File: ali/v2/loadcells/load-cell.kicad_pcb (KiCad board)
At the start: 4 copper layers, 85 x 76 mm, 108 parts, among them J1 Conn_02x01, J10 Conn_01x04, J11 Conn_01x04, J12 Conn_01x04, J2 Conn_01x05, J26 Vertical Ethernet, J3 USB_C_Receptacle_USB2.0_16P, J4 Conn_01x15, J5 Conn_02x09_Counter_Clockwise, J6 Screw_Terminal_01x02, J8 Conn_01x03, J9 Conn_01x04, SW1 SKRPANE010, U1 STM32H563RIV6, U2 AP2112K-3.3, U4 TJA1462ATK, U6 ADS124S08, U7 LAN8742AI, Y1 25 MHz, Y2 25 MHz

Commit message: Update LCs to have 6 inputs instead of 4
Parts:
- removed J10, J11, J9: Conn_01x04, APRL_Connector_Molex:Molex_CLIK-Mate_503159-0401_1x04-1MP_P1.50mm_Vertical
- added C51: 1nF, APRL_Passive:C_0603, F.Cu at (106.5, 80.5)
- added C52: 1nF, APRL_Passive:C_0603, F.Cu at (106.5, 74.8)
- added C53: 1nF, APRL_Passive:C_0603, F.Cu at (106.5, 99.7)
- added C54: 1nF, APRL_Passive:C_0603, F.Cu at (106.5, 93.7)
- added C55: 10nF, APRL_Passive:C_0603, F.Cu at (108.7, 77.5)
- added C56: 10nF, APRL_Passive:C_0603, F.Cu at (108.7, 96.7)
- added J13: Conn_01x04, APRL_Connector_Molex:Molex_CLIK-Mate_503159-0401_1x04-1MP_P1.50mm_Vertical, F.Cu at (98.9, 113.6)
- added J14: Conn_01x04, APRL_Connector_Molex:Molex_CLIK-Mate_503159-0401_1x04-1MP_P1.50mm_Vertical, F.Cu at (98.9, 104.1)
- added J15: Conn_01x04, APRL_Connector_Molex:Molex_CLIK-Mate_503159-0401_1x04-1MP_P1.50mm_Vertical, F.Cu at (99.0, 84.8)
- added J16: Conn_01x04, APRL_Connector_Molex:Molex_CLIK-Mate_503159-0401_1x04-1MP_P1.50mm_Vertical, F.Cu at (98.9, 75.2)
- added J17: Conn_01x04, APRL_Connector_Molex:Molex_CLIK-Mate_503159-0401_1x04-1MP_P1.50mm_Vertical, F.Cu at (98.9, 94.4)
- added R32: 4.7k, APRL_Passive:R_0603, F.Cu at (106.5, 78.5)
- added R33: 4.7k, APRL_Passive:R_0603, F.Cu at (106.5, 76.5)
- added R34: 4.7k, APRL_Passive:R_0603, F.Cu at (106.5, 97.7)
- added R35: 4.7k, APRL_Passive:R_0603, F.Cu at (106.5, 95.7)
- moved C37 13.2 mm to (106.5, 109.3), turned to 0 degrees
- moved R24 12.8 mm to (106.5, 107.3)
- moved C39 12.6 mm to (108.7, 106.3), turned to 90 degrees
- moved R25 12.4 mm to (106.5, 105.3)
- moved C38 12.0 mm to (106.5, 103.3), turned to 180 degrees
- moved C42 8.92 mm to (106.5, 118.9), turned to 0 degrees
- moved R26 8.53 mm to (106.5, 116.9)
- moved C44 8.33 mm to (108.7, 115.9), turned to 90 degrees
- moved R27 8.13 mm to (106.5, 114.9)
- moved C34 7.80 mm to (106.5, 90.1), turned to 0 degrees
- moved C43 7.73 mm to (106.5, 112.9), turned to 180 degrees
- moved R22 7.40 mm to (106.5, 88.1)
- moved C35 7.20 mm to (108.7, 87.1), turned to 90 degrees
- moved R23 7.00 mm to (106.5, 86.1)
- moved C36 6.61 mm to (106.5, 84.1), turned to 180 degrees
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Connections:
- C34 pad 1: Net-(U6-GPIO0/AIN8) -> GND
- C34 pad 2: GND -> Net-(U6-GPIO0/AIN8)
- C35 pad 1: Net-(U6-GPIO1/AIN9) -> Net-(U6-GPIO0/AIN8)
- C35 pad 2: Net-(U6-GPIO0/AIN8) -> Net-(U6-GPIO1/AIN9)
- C36 pad 1: GND -> Net-(U6-GPIO1/AIN9)
- C36 pad 2: Net-(U6-GPIO1/AIN9) -> GND
- C37 pad 1: Net-(U6-AIN4) -> GND
- C37 pad 2: GND -> Net-(U6-AIN4)
- C38 pad 1: GND -> Net-(U6-AIN5)
- C38 pad 2: Net-(U6-AIN5) -> GND
- C39 pad 1: Net-(U6-AIN5) -> Net-(U6-AIN4)
- C39 pad 2: Net-(U6-AIN4) -> Net-(U6-AIN5)
- C42 pad 1: Net-(U6-AIN2) -> GND
- C42 pad 2: GND -> Net-(U6-AIN2)
- C43 pad 1: GND -> Net-(U6-AIN3)
- C43 pad 2: Net-(U6-AIN3) -> GND
- C44 pad 1: Net-(U6-AIN3) -> Net-(U6-AIN2)
- C44 pad 2: Net-(U6-AIN2) -> Net-(U6-AIN3)
- C45 pad 1: Net-(U6-AIN0) -> GND
- C45 pad 2: GND -> Net-(U6-AIN0)
- C46 pad 1: GND -> Net-(U6-AIN1)
- C46 pad 2: Net-(U6-AIN1) -> GND
- C47 pad 1: Net-(U6-AIN1) -> Net-(U6-AIN0)
- C47 pad 2: Net-(U6-AIN0) -> Net-(U6-AIN1)
- J12 pad 1: +5V -> GND
- J12 pad 4: GND -> +5V
- R28 pad 1: Net-(J12-Pin_2) -> Net-(J12-Pin_3)
- R29 pad 1: Net-(J12-Pin_3) -> Net-(J12-Pin_2)
- U6 pad 19: unconnected-(U6-GPIO3/AIN11-Pad19) -> Net-(U6-GPIO3/AIN11)
- U6 pad 20: unconnected-(U6-GPIO2/AIN10-Pad20) -> Net-(U6-GPIO2/AIN10)
- U6 pad 31: unconnected-(U6-REFN1/AIN7-Pad31) -> Net-(U6-REFN1/AIN7)
- U6 pad 32: unconnected-(U6-REFP1/AIN6-Pad32) -> Net-(U6-REFP1/AIN6)
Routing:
- net Net-(U6-REFP1/AIN6): track 0.00 -> 24.0 mm
- net Net-(U6-REFN1/AIN7): track 0.00 -> 23.0 mm
- net Net-(U6-GPIO3/AIN11): track 0.00 -> 20.7 mm
- net Net-(U6-GPIO2/AIN10): track 0.00 -> 20.1 mm
- net Net-(U6-AIN4): track 21.1 -> 33.1 mm
- net Net-(U6-AIN5): track 19.3 -> 31.3 mm
- net Net-(U6-AIN2): track 35.5 -> 43.3 mm
- net Net-(U6-GPIO0/AIN8): track 18.3 -> 25.9 mm
- net Net-(U6-AIN3): track 33.8 -> 41.3 mm
- net Net-(U6-GPIO1/AIN9): track 19.0 -> 26.0 mm
- net Net-(J17-Pin_3): track 0.00 -> 6.92 mm
- net Net-(J16-Pin_3): track 0.00 -> 6.92 mm
- net +5V: track 86.6 -> 91.5 mm
- net Net-(J17-Pin_2): track 0.00 -> 4.92 mm
- net Net-(J16-Pin_2): track 0.00 -> 4.92 mm
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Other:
- board text added: "L5"
- board text added: "L6"

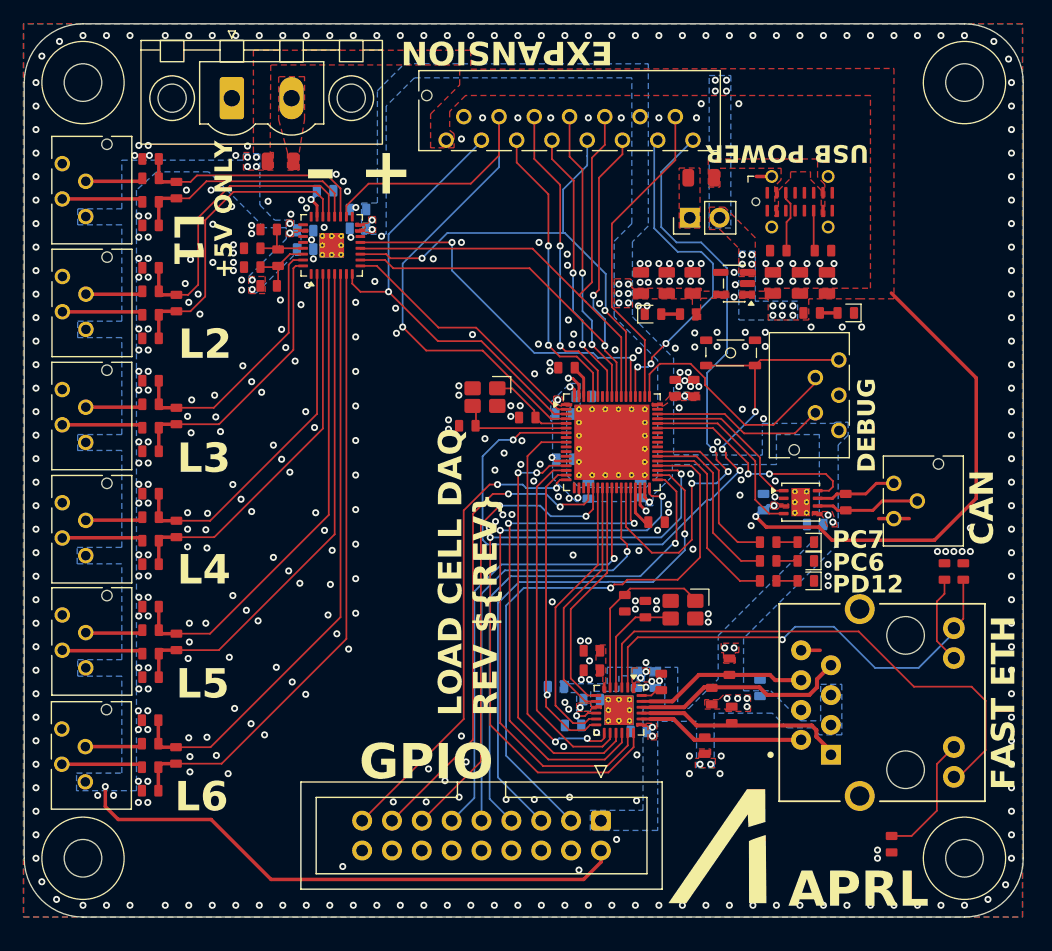
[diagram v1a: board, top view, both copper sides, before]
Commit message: Use 1206 on AFEs
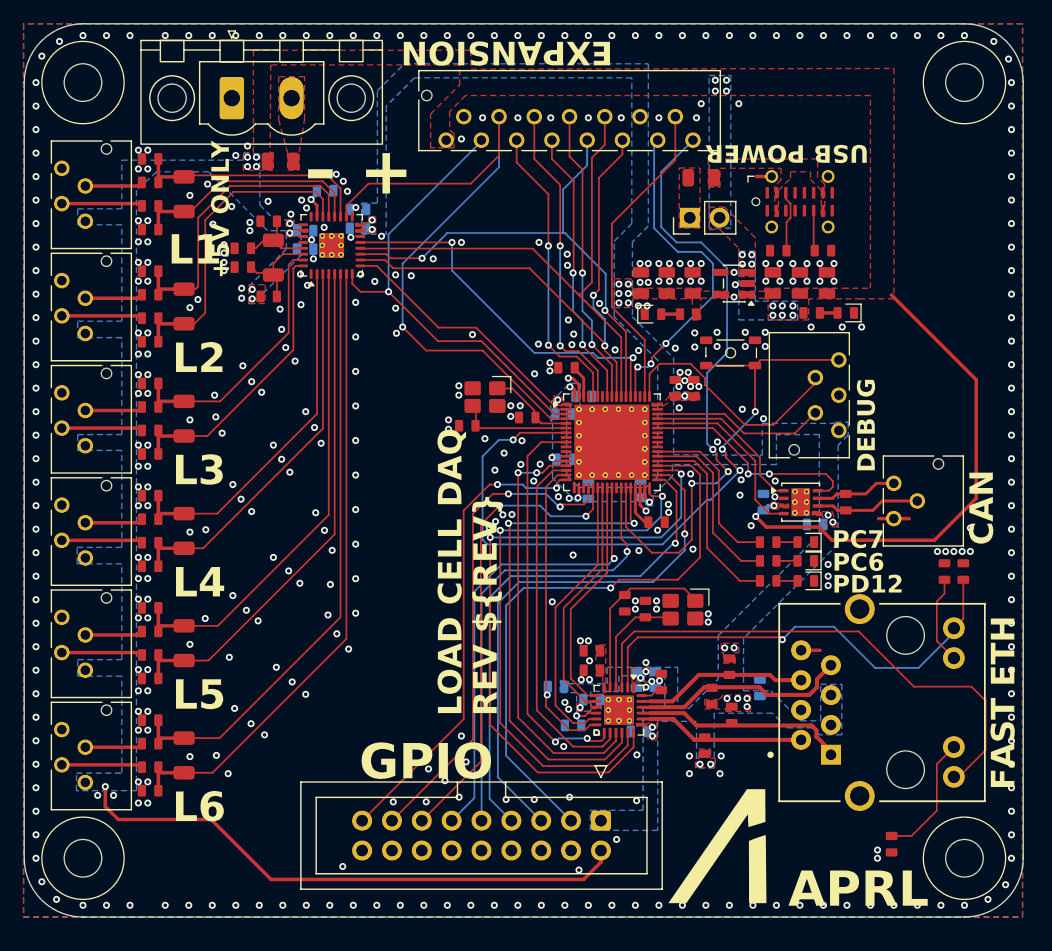
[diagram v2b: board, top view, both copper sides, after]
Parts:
- C35, C39, C44, C47, C50, C55, C56: footprint APRL_Passive:C_0603 -> APRL_Passive:C_1206
- moved R30 0.90 mm to (116.5, 86.5)
- moved C48 0.80 mm to (114.3, 84.0)
- moved C49 0.80 mm to (114.3, 82.4)
- moved C55 0.74 mm to (109.3, 77.8)
- moved C35 0.71 mm to (109.3, 87.4)
- moved R31 0.70 mm to (116.5, 80.1)
- moved C56 0.69 mm to (109.3, 96.9)
- moved C47 0.69 mm to (109.3, 125.6)
- moved C39 0.67 mm to (109.3, 106.5)
- moved C44 0.66 mm to (109.3, 116.0)
- moved J16 0.40 mm to (98.9, 75.6)
- moved C50 0.40 mm to (116.9, 83.2)
- moved J15 0.35 mm to (98.9, 85.2)
- moved C51 0.35 mm to (106.4, 80.8)
- moved R32 0.35 mm to (106.4, 78.8)
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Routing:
- net Net-(U6-REFP0): track 5.82 -> 7.90 mm
- net Net-(U6-GPIO0/AIN8): track 25.9 -> 27.4 mm
- net Net-(U6-REFN0): track 5.31 -> 6.73 mm
- net Net-(U6-AIN0): track 53.6 -> 54.3 mm
- net Net-(U6-GPIO2/AIN10): track 20.1 -> 20.8 mm
- net Net-(U6-REFP1/AIN6): track 24.0 -> 24.7 mm
- net Net-(U6-AIN4): track 33.1 -> 33.7 mm
- net Net-(U6-AIN2): track 43.3 -> 43.9 mm
- net GND: vias 470 -> 460
